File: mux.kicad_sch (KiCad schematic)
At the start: 22 parts, among them M1 SN74LV4051ADYYR, M10 SN74LV4051ADYYR, M11 SN74LV4051ADYYR, M2 SN74LV4051ADYYR, M3 SN74LV4051ADYYR, M4 SN74LV4051ADYYR, M5 SN74LV4051ADYYR, M6 SN74LV4051ADYYR, M7 SN74LV4051ADYYR, M8 SN74LV4051ADYYR, M9 SN74LV4051ADYYR

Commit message: caca
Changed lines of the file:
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@@
-		)
-	)
-	(global_label "K26_OUT"
-		(shape input)
-		(at 85.09 99.06 0)
-		(fields_autoplaced yes)
-		(effects
-			(font
-				(size 1.27 1.27)
-			)
-			(justify left)
-		)
-		(property "Intersheetrefs" "${INTERSHEET_REFS}"
-			(at 96.3604 99.06 0)
-			(effects
-				(font
-					(size 1.27 1.27)
-				)
-				(justify left)
-				(hide yes)
-			)
 		)
 	)

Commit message: Update 0402 resistors to 680Ω and add libs
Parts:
- M1, M10, M11, M2, M3, M4, M5, M6, M7, M8, M9: footprint SOT-23-THIN16_DYY_TEX -> SN74LV4051ADYYR:SOT-23-THIN16_DYY_TEX

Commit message: fix: add missing 3d models
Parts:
- M1, M10, M11, M2, M3, M4, M5, M6, M7, M8, M9: footprint SN74LV4051ADYYR:SOT-23-THIN16_DYY_TEX -> SOT-23-THIN16_DYY_TEX
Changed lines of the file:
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@@
 			)
 		)
-		(property "Footprint" "SN74LV4051ADYYR:SOT-23-THIN16_DYY_TEX"
+		(property "Footprint" "SOT-23-THIN16_DYY_TEX"
 			(at 116.84 185.42 0)
 			(effects
@@
 	)
 	(symbol
+		(lib_name "SN74LV4051ADYYR_1")
 		(lib_id "SN74LV4051ADYYR:SN74LV4051ADYYR")
 		(at 29.21 29.21 0)
@@
 			)
 		)
-		(property "Footprint" "SN74LV4051ADYYR:SOT-23-THIN16_DYY_TEX"
+		(property "Footprint" "SOT-23-THIN16_DYY_TEX"
 			(at 29.21 29.21 0)
 			(effects
@@
 			)
 		)
-		(property "Footprint" "SN74LV4051ADYYR:SOT-23-THIN16_DYY_TEX"
+		(property "Footprint" "SOT-23-THIN16_DYY_TEX"
 			(at 116.84 29.21 0)
 			(effects
@@
 			)
 		)
-		(property "Footprint" "SN74LV4051ADYYR:SOT-23-THIN16_DYY_TEX"
+		(property "Footprint" "SOT-23-THIN16_DYY_TEX"
 			(at 29.21 133.35 0)
 			(effects
@@
 			)
 		)
-		(property "Footprint" "SN74LV4051ADYYR:SOT-23-THIN16_DYY_TEX"
+		(property "Footprint" "SOT-23-THIN16_DYY_TEX"
 			(at 196.85 29.21 0)
 			(effects
@@
 			)
 		)
-		(property "Footprint" "SN74LV4051ADYYR:SOT-23-THIN16_DYY_TEX"
+		(property "Footprint" "SOT-23-THIN16_DYY_TEX"
 			(at 116.84 81.28 0)
 			(effects
@@
 			)
 		)
-		(property "Footprint" "SN74LV4051ADYYR:SOT-23-THIN16_DYY_TEX"
+		(property "Footprint" "SOT-23-THIN16_DYY_TEX"
 			(at 116.84 133.35 0)
 			(effects
@@
 			)
 		)
-		(property "Footprint" "SN74LV4051ADYYR:SOT-23-THIN16_DYY_TEX"
+		(property "Footprint" "SOT-23-THIN16_DYY_TEX"
 			(at 29.21 185.42 0)
 			(effects
@@
 			)
 		)
-		(property "Footprint" "SN74LV4051ADYYR:SOT-23-THIN16_DYY_TEX"
+		(property "Footprint" "SOT-23-THIN16_DYY_TEX"
 			(at 29.21 81.28 0)
 			(effects
@@
 			)
 		)
-		(property "Footprint" "SN74LV4051ADYYR:SOT-23-THIN16_DYY_TEX"
+		(property "Footprint" "SOT-23-THIN16_DYY_TEX"
 			(at 196.85 133.35 0)
 			(effects
@@
 			)
 		)
-		(property "Footprint" "SN74LV4051ADYYR:SOT-23-THIN16_DYY_TEX"
+		(property "Footprint" "SOT-23-THIN16_DYY_TEX"
 			(at 196.85 81.28 0)
 			(effects

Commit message: Placed led
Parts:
- renumbered C201 to C186, C205 to C187, C211 to C188, C202 to C189, C206 to C190, C212 to C191, C203 to C192, C209 to C193, C213 to C194, C204 to C195, C210 to C196, M4 to M10, M8 to M11, M5 to M2, M9 to M3, M2 to M4, M6 to M5, M10 to M6, M3 to M7, M7 to M8, M11 to M9

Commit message: led capacitor & sensor capacitor & fixes
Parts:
- M1, M10, M11, M2, M3, M4, M5, M6, M7, M8, M9: footprint SOT-23-THIN16_DYY_TEX -> SN74LV4051ADYYR:SOT-23-THIN16_DYY_TEX
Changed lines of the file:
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@@
 			)
 		)
-		(property "Footprint" "SOT-23-THIN16_DYY_TEX"
+		(property "Footprint" "SN74LV4051ADYYR:SOT-23-THIN16_DYY_TEX"
 			(at 116.84 185.42 0)
 			(hide yes)
@@
 			)
 		)
-		(property "Footprint" "SOT-23-THIN16_DYY_TEX"
+		(property "Footprint" "SN74LV4051ADYYR:SOT-23-THIN16_DYY_TEX"
 			(at 29.21 29.21 0)
 			(hide yes)
@@
 			)
 		)
-		(property "Footprint" "SOT-23-THIN16_DYY_TEX"
+		(property "Footprint" "SN74LV4051ADYYR:SOT-23-THIN16_DYY_TEX"
 			(at 116.84 29.21 0)
 			(hide yes)
@@
 			)
 		)
-		(property "Footprint" "SOT-23-THIN16_DYY_TEX"
+		(property "Footprint" "SN74LV4051ADYYR:SOT-23-THIN16_DYY_TEX"
 			(at 29.21 133.35 0)
 			(hide yes)
@@
 			)
 		)
-		(property "Footprint" "SOT-23-THIN16_DYY_TEX"
+		(property "Footprint" "SN74LV4051ADYYR:SOT-23-THIN16_DYY_TEX"
 			(at 196.85 29.21 0)
 			(hide yes)
@@
 			)
 		)
-		(property "Footprint" "SOT-23-THIN16_DYY_TEX"
+		(property "Footprint" "SN74LV4051ADYYR:SOT-23-THIN16_DYY_TEX"
 			(at 116.84 81.28 0)
 			(hide yes)
@@
 			)
 		)
-		(property "Footprint" "SOT-23-THIN16_DYY_TEX"
+		(property "Footprint" "SN74LV4051ADYYR:SOT-23-THIN16_DYY_TEX"
 			(at 116.84 133.35 0)
 			(hide yes)
@@
 			)
 		)
-		(property "Footprint" "SOT-23-THIN16_DYY_TEX"
+		(property "Footprint" "SN74LV4051ADYYR:SOT-23-THIN16_DYY_TEX"
 			(at 29.21 185.42 0)
 			(hide yes)
@@
 			)
 		)
-		(property "Footprint" "SOT-23-THIN16_DYY_TEX"
+		(property "Footprint" "SN74LV4051ADYYR:SOT-23-THIN16_DYY_TEX"
 			(at 29.21 81.28 0)
 			(hide yes)
@@
 			)
 		)
-		(property "Footprint" "SOT-23-THIN16_DYY_TEX"
+		(property "Footprint" "SN74LV4051ADYYR:SOT-23-THIN16_DYY_TEX"
 			(at 196.85 133.35 0)
 			(hide yes)
@@
 			)
 		)
-		(property "Footprint" "SOT-23-THIN16_DYY_TEX"
+		(property "Footprint" "SN74LV4051ADYYR:SOT-23-THIN16_DYY_TEX"
 			(at 196.85 81.28 0)
 			(hide yes)

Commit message: lcsc part
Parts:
- M1, M10, M11, M2, M3, M4, M5, M6, M7, M8, M9: LCSC (none) -> C41558096
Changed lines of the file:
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@@
 			)
 		)
+		(property "LCSC" "C41558096"
+			(at 116.84 185.42 0)
+			(hide yes)
+			(show_name no)
+			(do_not_autoplace no)
+			(effects
+				(font
+					(size 1.27 1.27)
+				)
+			)
+		)
 		(pin "9"
 		)
@@
 			)
 		)
+		(property "LCSC" "C41558096"
+			(at 29.21 29.21 0)
+			(hide yes)
+			(show_name no)
+			(do_not_autoplace no)
+			(effects
+				(font
+					(size 1.27 1.27)
+				)
+			)
+		)
 		(pin "9"
 		)
@@
 			)
 		)
+		(property "LCSC" "C41558096"
+			(at 116.84 29.21 0)
+			(hide yes)
+			(show_name no)
+			(do_not_autoplace no)
+			(effects
+				(font
+					(size 1.27 1.27)
+				)
+			)
+		)
 		(pin "9"
 		)
@@
 			)
 		)
+		(property "LCSC" "C41558096"
+			(at 29.21 133.35 0)
+			(hide yes)
+			(show_name no)
+			(do_not_autoplace no)
+			(effects
+				(font
+					(size 1.27 1.27)
+				)
+			)
+		)
 		(pin "9"
 		)
@@
 			)
 		)
+		(property "LCSC" "C41558096"
+			(at 196.85 29.21 0)
+			(hide yes)
+			(show_name no)
+			(do_not_autoplace no)
+			(effects
+				(font
+					(size 1.27 1.27)
+				)
+			)
+		)
 		(pin "9"
 		)
@@
 			)
 		)
+		(property "LCSC" "C41558096"
+			(at 116.84 81.28 0)
+			(hide yes)
+			(show_name no)
+			(do_not_autoplace no)
+			(effects
+				(font
+					(size 1.27 1.27)
+				)
+			)
+		)
 		(pin "9"
 		)
@@
 			)
 		)
+		(property "LCSC" "C41558096"
+			(at 116.84 133.35 0)
+			(hide yes)
+			(show_name no)
+			(do_not_autoplace no)
+			(effects
+				(font
+					(size 1.27 1.27)
+				)
+			)
+		)
 		(pin "9"
 		)
@@
 			)
 		)
+		(property "LCSC" "C41558096"
+			(at 29.21 185.42 0)
+			(hide yes)
+			(show_name no)
+			(do_not_autoplace no)
+			(effects
+				(font
+					(size 1.27 1.27)
+				)
+			)
+		)
 		(pin "9"
 		)
@@
 			)
 		)
+		(property "LCSC" "C41558096"
+			(at 29.21 81.28 0)
+			(hide yes)
+			(show_name no)
+			(do_not_autoplace no)
+			(effects
+				(font
+					(size 1.27 1.27)
+				)
+			)
+		)
 		(pin "9"
 		)
@@
 			)
 		)
+		(property "LCSC" "C41558096"
+			(at 196.85 133.35 0)
+			(hide yes)
+			(show_name no)
+			(do_not_autoplace no)
+			(effects
+				(font
+					(size 1.27 1.27)
+				)
+			)
+		)
 		(pin "9"
 		)
@@
 			(at 196.85 81.28 0)
 			(hide yes)
+			(show_name no)
+			(do_not_autoplace no)
+			(effects
+				(font
+					(size 1.27 1.27)
+				)
+			)
+		)
+		(property "LCSC" "C41558096"
+			(at 196.85 81.28 0)
+			(hide yes)

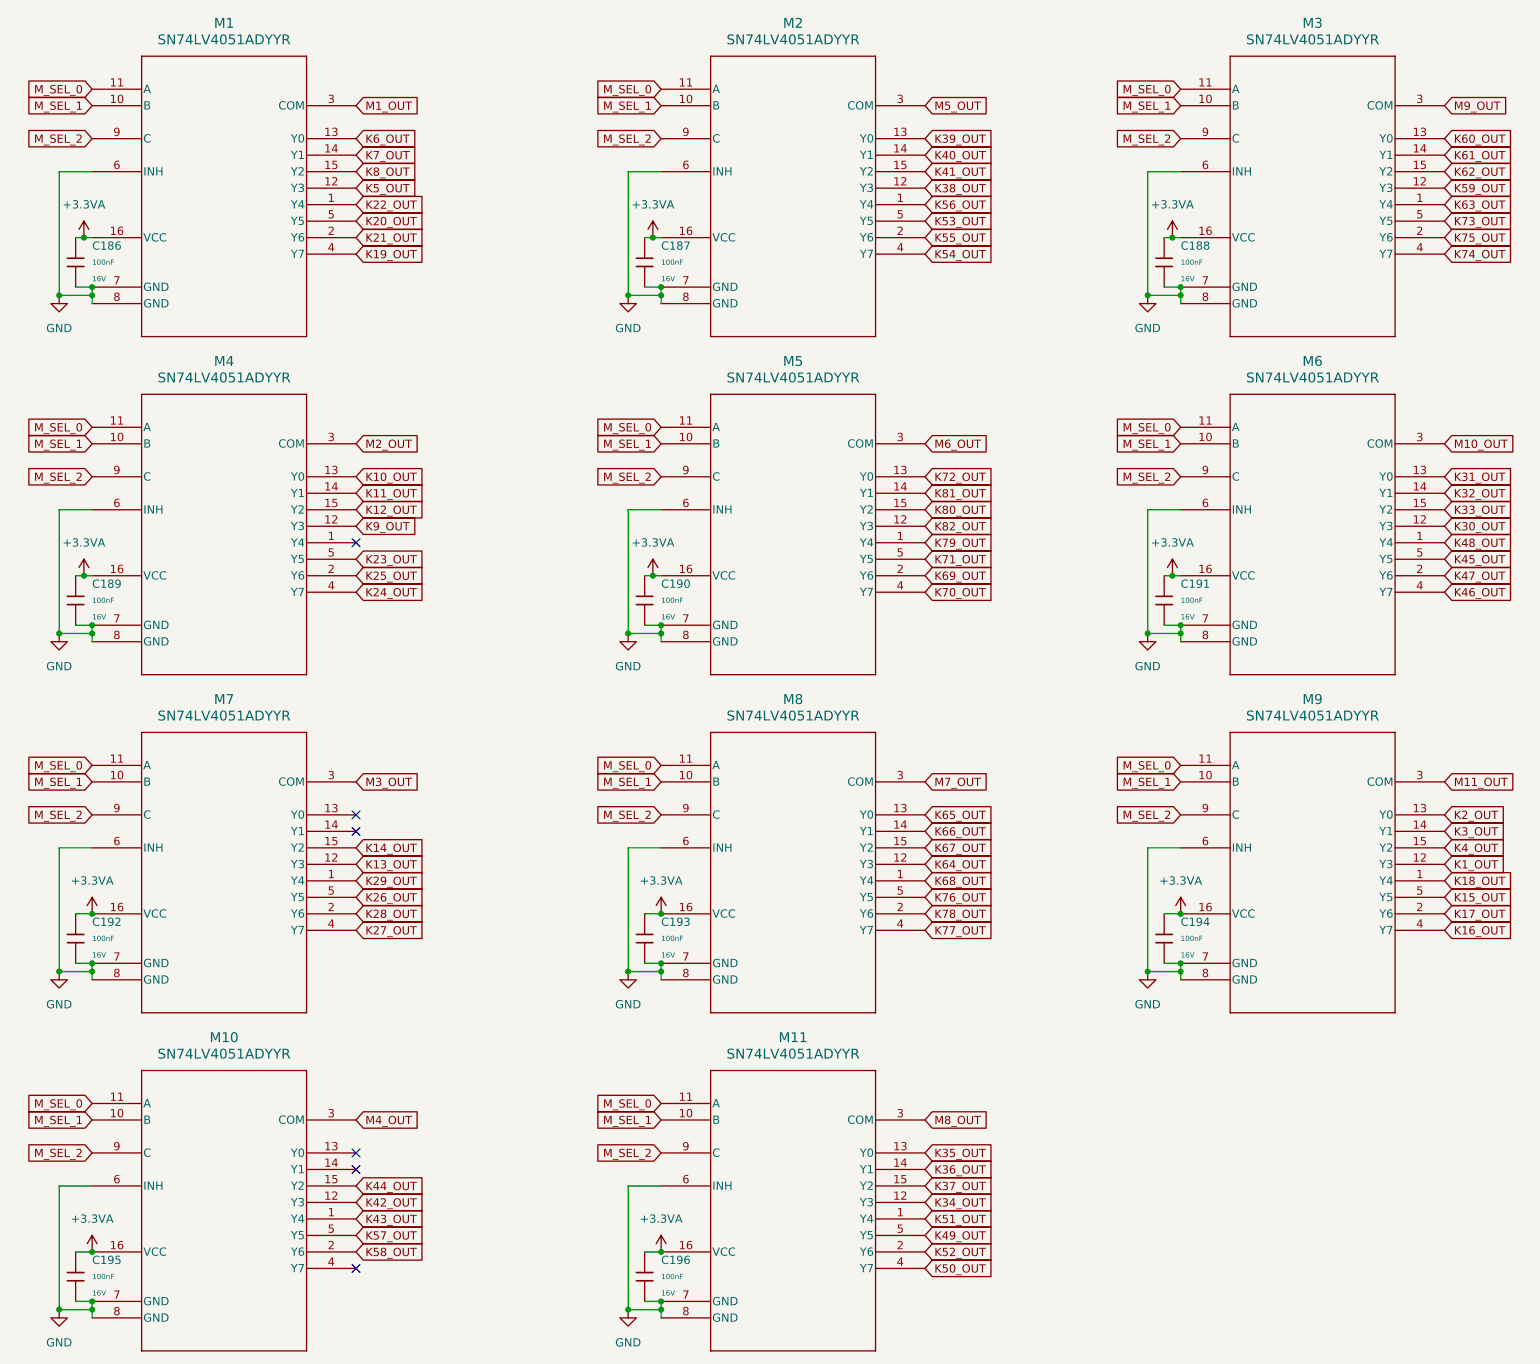
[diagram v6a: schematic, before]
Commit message: route sensors to mux & data led
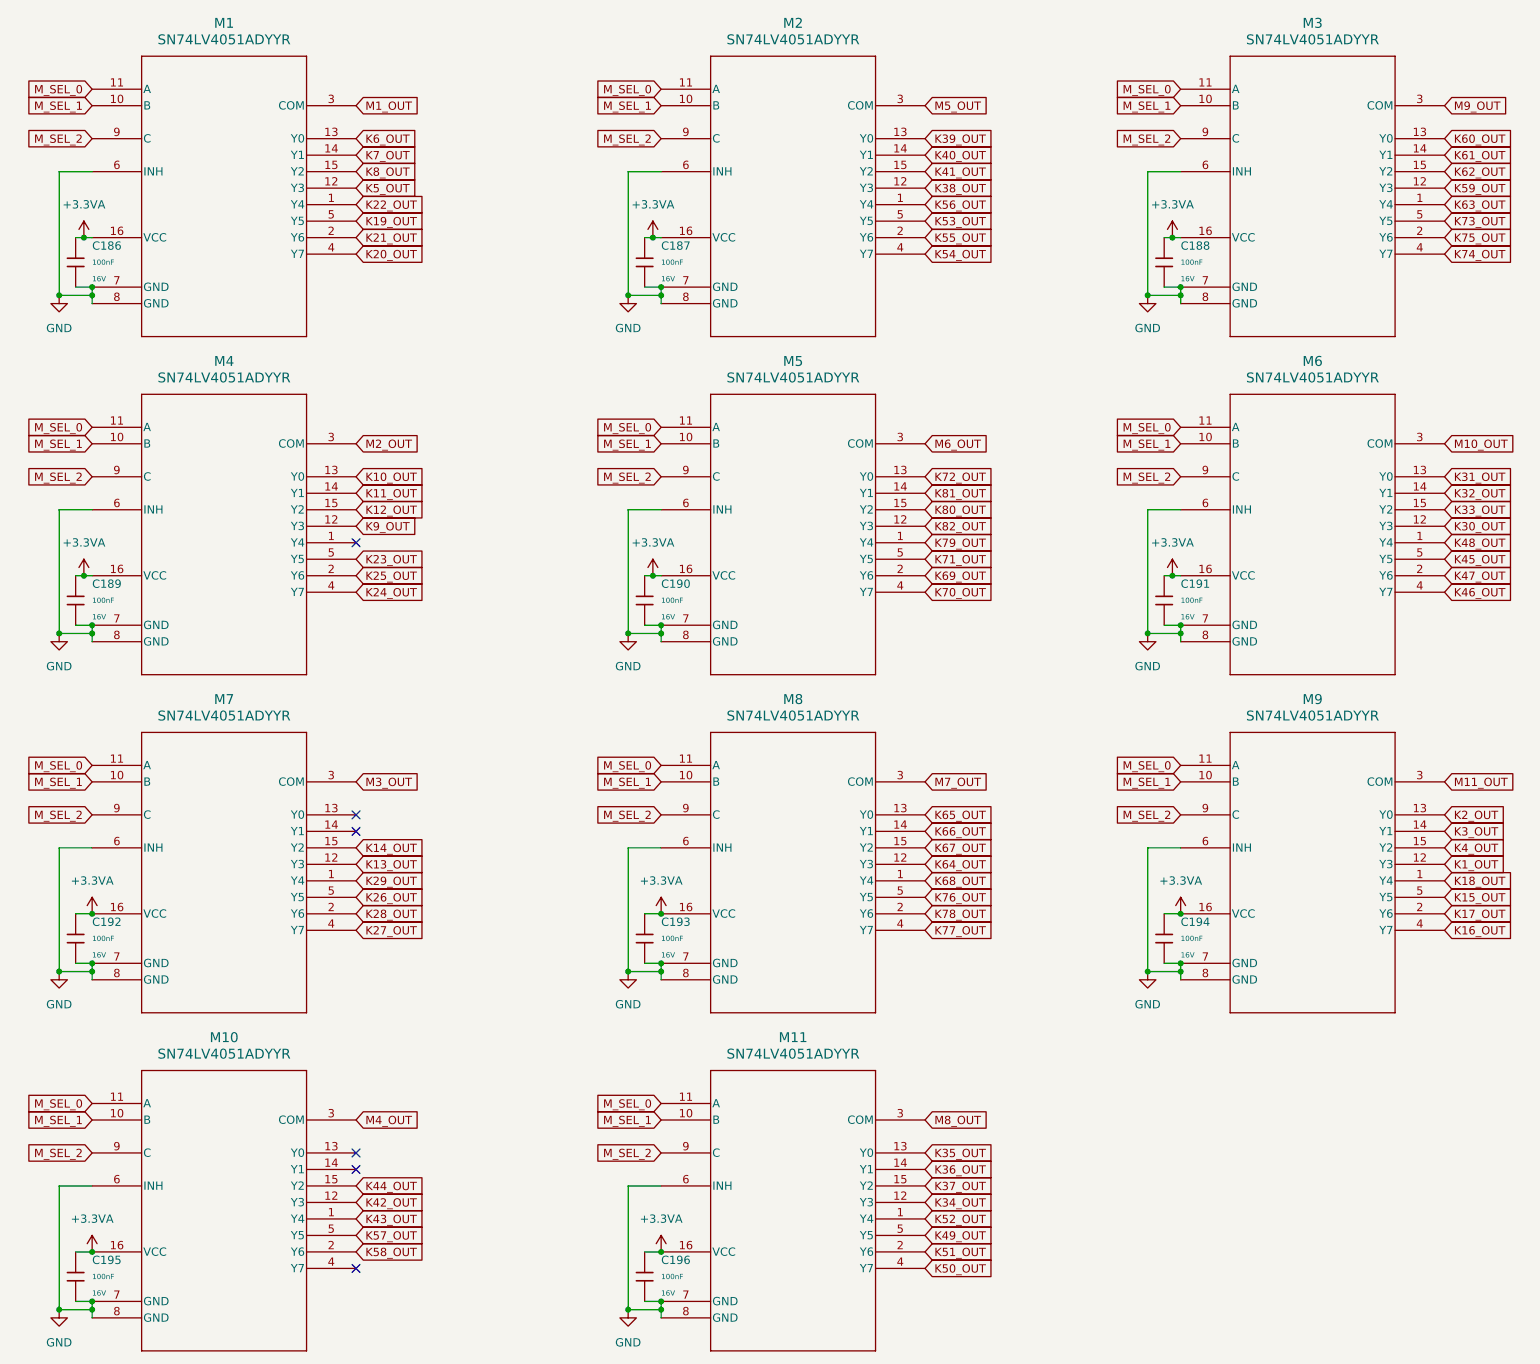
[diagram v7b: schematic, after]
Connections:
- net K19_OUT: now also M1.5 (Y5); no longer M1.4 (Y7)
- net K20_OUT: now also M1.4 (Y7); no longer M1.5 (Y5)
- net K51_OUT: now also M11.2 (Y6); no longer M11.1 (Y4)
- net K52_OUT: now also M11.1 (Y4); no longer M11.2 (Y6)

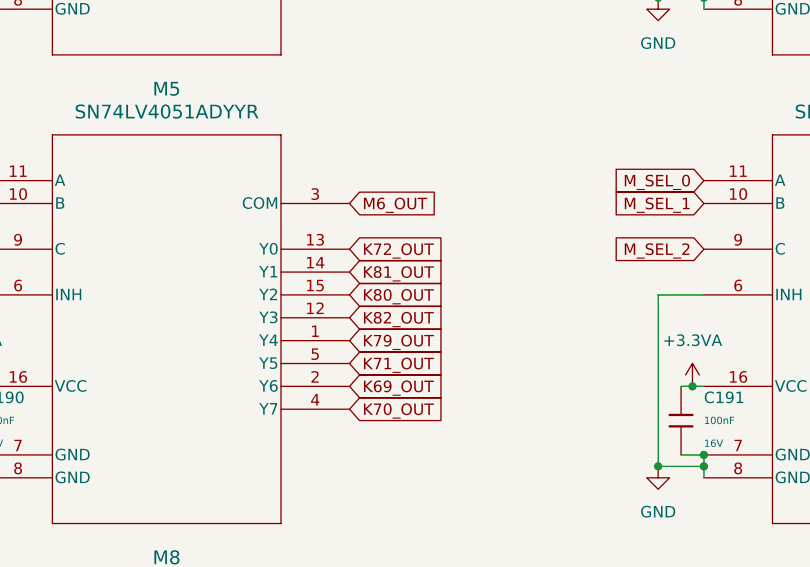
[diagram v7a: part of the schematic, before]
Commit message: add jlc drc & route mux select
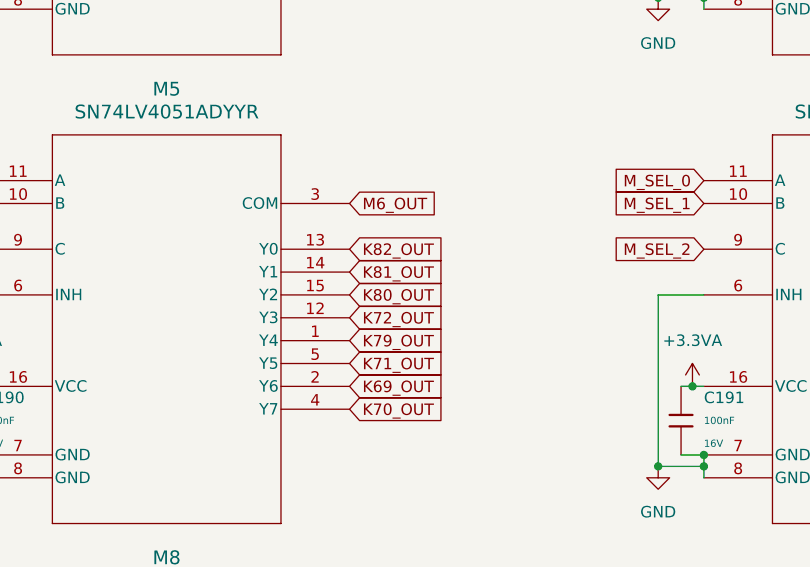
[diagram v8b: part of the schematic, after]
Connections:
- net K72_OUT: now also M5.12 (Y3); no longer M5.13 (Y0)
- net K82_OUT: now also M5.13 (Y0); no longer M5.12 (Y3)
